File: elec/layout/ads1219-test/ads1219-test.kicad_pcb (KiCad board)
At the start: 2 copper layers, 24 parts

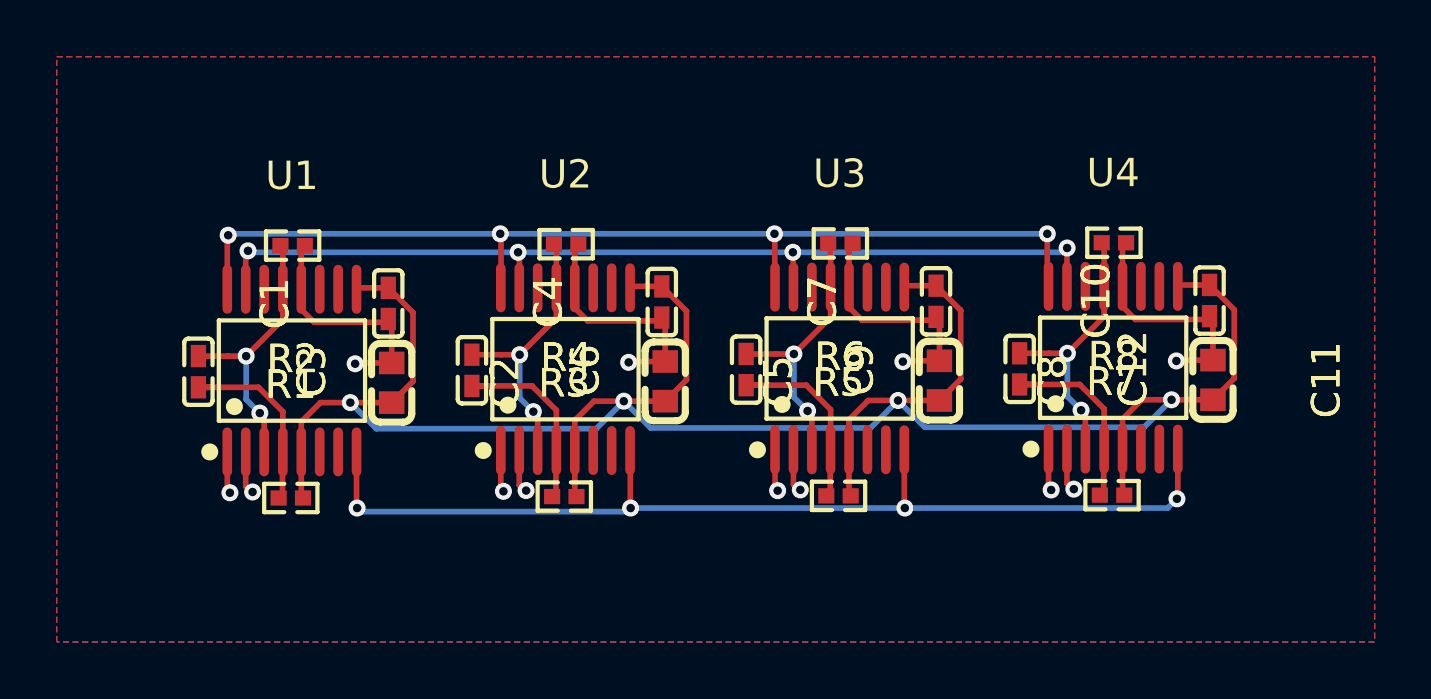
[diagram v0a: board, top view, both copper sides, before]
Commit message: updates for i2c addressing
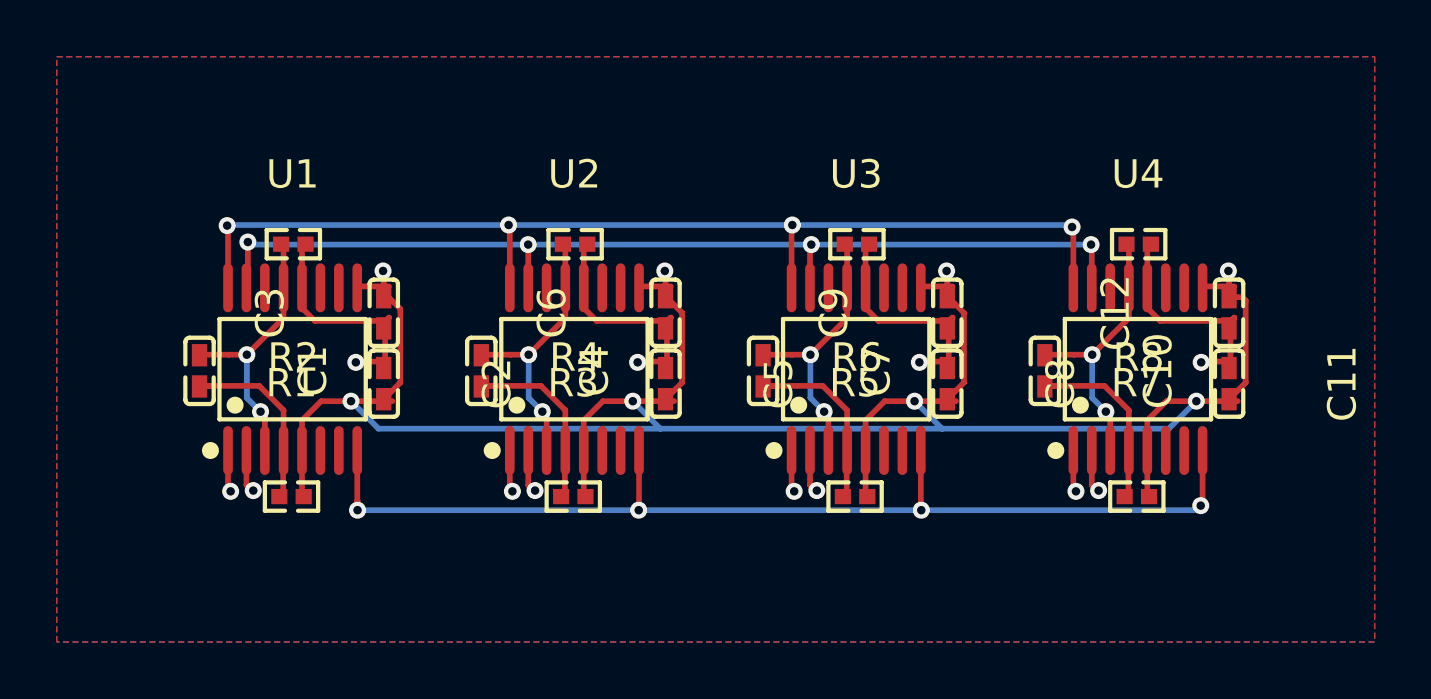
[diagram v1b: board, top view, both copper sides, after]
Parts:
- C1, C10, C12, C3, C4, C6, C7, C9: value 100nF ±10% 16V X7R -> 1µF ±10% 25V X5R
- C11, C2, C5, C8: value 10µF ±10% 10V X5R -> 1µF ±10% 25V X5R; footprint atopile:C0603-bd72f6 -> atopile:C0402-b3ef17
- moved C12 7.65 mm to (171.4, 90.3), turned to 90 degrees
- moved C9 7.38 mm to (161.5, 90.3), turned to 90 degrees
- moved C6 7.13 mm to (151.6, 90.3), turned to 90 degrees
- moved C1 7.07 mm to (135.1, 92.4), turned to -90 degrees
- moved C3 6.86 mm to (141.6, 90.3), turned to 90 degrees
- moved C4 6.82 mm to (145.1, 92.4), turned to -90 degrees
- moved C7 6.58 mm to (155.0, 92.4), turned to -90 degrees
- moved C10 6.32 mm to (164.9, 92.4), turned to -90 degrees
- moved R8 0.88 mm to (168.2, 87.9)
- moved R7 0.88 mm to (168.2, 96.8)
- moved U4 0.88 mm to (168.2, 92.3)
- moved C11 0.58 mm to (171.4, 92.8)
- moved R6 0.58 mm to (158.3, 87.9)
- moved U3 0.58 mm to (158.3, 92.3)
- moved R5 0.58 mm to (158.2, 96.8)
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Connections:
- net adc1-AIN0 renamed adcs[0]-AIN0
- net adc1-AIN1 renamed adcs[0]-AIN1
- net adc1-AIN2 renamed adcs[0]-AIN2
- net adc1-AIN3 renamed adcs[0]-AIN3
- net adc1.ic-DRDYh renamed adcs[0].ic-DRDYh
- net adc2-AIN0 renamed adcs[1]-AIN0
- net adc2-AIN1 renamed adcs[1]-AIN1
- net adc2-AIN2 renamed adcs[1]-AIN2
- net adc2-AIN3 renamed adcs[1]-AIN3
- net adc2.ic-DRDYh renamed adcs[1].ic-DRDYh
- net adc3-AIN0 renamed adcs[2]-AIN0
- net adc3-AIN1 renamed adcs[2]-AIN1
- net adc3-AIN2 renamed adcs[2]-AIN2
- net adc3-AIN3 renamed adcs[2]-AIN3
- net adc3.ic-DRDYh renamed adcs[2].ic-DRDYh
- net adc4-AIN0 renamed adcs[3]-AIN0
- net adc4-AIN1 renamed adcs[3]-AIN1
- net adc4-AIN2 renamed adcs[3]-AIN2
- net adc4-AIN3 renamed adcs[3]-AIN3
- net adc4.ic-DRDYh renamed adcs[3].ic-DRDYh
- C1 pad 1: hv-1 -> hv-2
- C1 pad 2: gnd -> gnd-1
- C10 pad 2: gnd -> gnd-1
- C11 pad 1: hv-2 -> hv
- C12 pad 1: hv-4 -> hv
- C12 pad 2: gnd-1 -> gnd
- C2 pad 1: hv-1 -> hv-4
- C3 pad 2: gnd-1 -> gnd
- C4 pad 1: hv -> hv-2
- C4 pad 2: gnd -> gnd-1
- C5 pad 1: hv -> hv-1
- C6 pad 1: hv-4 -> hv-1
- C6 pad 2: gnd-1 -> gnd
- C7 pad 1: hv-3 -> hv-2
- C7 pad 2: gnd -> gnd-1
- C9 pad 1: hv-4 -> hv-3
- C9 pad 2: gnd-1 -> gnd
- R2 pad 1: hv-1 -> hv-4
- R2 pad 2: hv-4 -> hv-2
- R4 pad 1: hv -> hv-1
- R4 pad 2: hv-4 -> hv-2
- R6 pad 2: hv-4 -> hv-2
- R8 pad 1: hv-2 -> hv
- R8 pad 2: hv-4 -> hv-2
- U1 pad 12: hv-1 -> hv-4
- U1 pad 13: hv-4 -> hv-2
- U1 pad 3: hv-4 -> hv-2
- U2 pad 1: hv-4 -> hv-2
- U2 pad 12: hv -> hv-1
- U2 pad 13: hv-4 -> hv-2
- U2 pad 3: hv-4 -> hv-2
- U3 pad 13: hv-4 -> hv-2
- U3 pad 2: hv-4 -> hv-2
- U3 pad 3: hv-4 -> hv-2
- U4 pad 1: hv-4 -> hv-2
- U4 pad 12: hv-2 -> hv
- U4 pad 13: hv-4 -> hv-2
- U4 pad 2: hv-4 -> hv-2
- U4 pad 3: hv-4 -> hv-2
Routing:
- net hv-4: track 45.2 -> 8.30 mm, vias 12 -> 1
- net hv-2: track 8.51 -> 45.2 mm, vias 1 -> 12
- net gnd: track 79.5 -> 83.2 mm, vias 4 -> 8
- net SCL: track 36.4 -> 38.7 mm
- net SDA: track 34.2 -> 36.0 mm
- net REFN: track 37.1 -> 38.1 mm
- added copper zone on B.Cu, net hv-2
- removed copper zone on B.Cu, net hv-4

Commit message: questionable progress
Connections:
- net hv-1 renamed adcs[1]-AVDD
- net hv-3 renamed adcs[2]-AVDD
- net hv-4 renamed adcs[0]-AVDD
- C1 pad 1: hv-2 -> hv
- C10 pad 1: hv-2 -> hv
- C11 pad 1: hv -> adcs[3]-AVDD
- C11 pad 2: gnd -> adcs[3]-gnd
- C12 pad 1: hv -> adcs[3]-AVDD
- C12 pad 2: gnd -> adcs[3]-gnd
- C2 pad 2: gnd -> adcs[0]-gnd
- C3 pad 2: gnd -> adcs[0]-gnd
- C4 pad 1: hv-2 -> hv
- C5 pad 2: gnd -> adcs[1]-gnd
- C6 pad 2: gnd -> adcs[1]-gnd
- C7 pad 1: hv-2 -> hv
- C8 pad 2: gnd -> adcs[2]-gnd
- C9 pad 2: gnd -> adcs[2]-gnd
- R1 pad 2: gnd -> adcs[0]-gnd
- R2 pad 2: hv-2 -> hv
- R3 pad 2: gnd -> adcs[1]-gnd
- R4 pad 2: hv-2 -> hv
- R5 pad 2: gnd -> adcs[2]-gnd
- R6 pad 2: hv-2 -> hv
- R7 pad 2: gnd -> adcs[3]-gnd
- R8 pad 1: hv -> adcs[3]-AVDD
- R8 pad 2: hv-2 -> hv
- U1 pad 13: hv-2 -> hv
- U1 pad 3: hv-2 -> hv
- U1 pad 5: gnd -> adcs[0]-gnd
- U2 pad 1: hv-2 -> hv
- U2 pad 13: hv-2 -> hv
- U2 pad 3: hv-2 -> hv
- U2 pad 5: gnd -> adcs[1]-gnd
- U3 pad 13: hv-2 -> hv
- U3 pad 2: hv-2 -> hv
- U3 pad 3: hv-2 -> hv
- U3 pad 5: gnd -> adcs[2]-gnd
- U4 pad 1: hv-2 -> hv
- U4 pad 12: hv -> adcs[3]-AVDD
- U4 pad 13: hv-2 -> hv
- U4 pad 2: hv-2 -> hv
- U4 pad 3: hv-2 -> hv
- U4 pad 5: gnd -> adcs[3]-gnd
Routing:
- net gnd: track 83.2 -> 0.00 mm, vias 8 -> 0
- net adcs[1]-gnd: track 0.00 -> 83.2 mm, vias 0 -> 8
- net hv-2: track 45.2 -> 0.00 mm, vias 12 -> 0
- net hv: track 8.30 -> 45.2 mm, vias 1 -> 12
- net adcs[3]-AVDD: track 0.00 -> 8.30 mm, vias 0 -> 1
- added copper zone on B.Cu, net hv
- removed copper zone on B.Cu, net hv-2
